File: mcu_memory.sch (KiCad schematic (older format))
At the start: 43 parts, among them J1 Conn_02x03_Odd_Even, P10 CONN_02X20, U2 STM32F429IGTx

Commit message: Corrected pinout of lateral IDC 40 pin. Moved other bits to another port
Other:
- note added: "OPTIMIZED FOR BUS ACCESS"
- note added: "PORTD 8 pins (SHIELD)"
- note added: "PORTE 6 pins (SHIELD)"
- note removed: "PORTD 13 pins (SHIELD)"
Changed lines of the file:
@@
 NoConn ~ 9900 5050
 NoConn ~ 9900 5150
-NoConn ~ 9900 8750
-NoConn ~ 9900 8850
-NoConn ~ 9900 8950
-NoConn ~ 9900 9050
-NoConn ~ 9900 9150
 NoConn ~ 9900 9250
 NoConn ~ 9900 9350
@@
 Text Notes 3400 8675 1    60   ~ 12
 PORTG 8 bit
-Text Notes 10425 8200 1    60   ~ 12
-PORTD 13 pins (SHIELD)
+Text Notes 10450 7900 1    60   ~ 12
+PORTD 8 pins (SHIELD)
 Wire Notes Line
 	3525 8950 3425 8950
@@
 Wire Notes Line
 	1050 7400 1050 10650
-Text GLabel 9900 7850 2    39   BiDi ~ 0
+Text GLabel 9900 8750 2    39   BiDi ~ 0
 D8
-Text GLabel 9900 7950 2    39   BiDi ~ 0
+Text GLabel 9900 8850 2    39   BiDi ~ 0
 D9
-Text GLabel 9900 8050 2    39   BiDi ~ 0
+Text GLabel 9900 8950 2    39   BiDi ~ 0
 D10
-Text GLabel 9900 8150 2    39   BiDi ~ 0
+Text GLabel 9900 9050 2    39   BiDi ~ 0
 D11
-Text GLabel 9900 8250 2    39   BiDi ~ 0
+Text GLabel 9900 9150 2    39   BiDi ~ 0
 D12
-Wire Notes Line
-	10075 7050 10300 7050
-Wire Notes Line
-	10300 7050 10300 8250
-Wire Notes Line
-	10300 8250 10125 8250
+NoConn ~ 9900 7850
+NoConn ~ 9900 7950
+NoConn ~ 9900 8050
+NoConn ~ 9900 8150
+NoConn ~ 9900 8250
+Wire Notes Line
+	10075 7050 10325 7050
+Wire Notes Line
+	10325 7050 10325 7750
+Wire Notes Line
+	10325 7750 10075 7750
+Wire Notes Line
+	10100 8750 10325 8750
+Wire Notes Line
+	10325 8750 10325 9150
+Wire Notes Line
+	10325 9150 10100 9150
+Text Notes 10475 9475 1    60   ~ 12
+PORTE 6 pins (SHIELD)
+Text Notes 10625 8000 1    59   ~ 12
+OPTIMIZED FOR BUS ACCESS
 $EndSCHEMATC

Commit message: Porting from Kicad 4 to Kicad 5
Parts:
- BOOT0_MEM1, BOOT1_MEM1: footprint Pin_Headers:Pin_Header_Straight_1x02 -> Connector_PinHeader_2.54mm:PinHeader_1x02_P2.54mm_Vertical; symbol CONN_01X02 -> stduinof429-rescue:CONN_01X02
- C10, C11, C12, C13, C14, C15, C16, C17, C18, C19, C20, C21, C22, C23, C24, C25, C26, C5, C6, C7, C8, C9: footprint Capacitors_SMD:C_1206_HandSoldering -> Capacitor_SMD:C_1206_3216Metric_Pad1.42x1.75mm_HandSolder; symbol C_Small -> Device1:C_Small
- D2: footprint LEDs:LED_1206 -> LED_SMD:LED_1206_3216Metric_Pad1.42x1.75mm_HandSolder; symbol Led_Small -> stduinof429-rescue:Led_Small
- DEBUG1: footprint Pin_Headers:Pin_Header_Straight_1x03 -> Connector_PinHeader_2.54mm:PinHeader_1x03_P2.54mm_Vertical; symbol CONN_01X03 -> stduinof429-rescue:CONN_01X03
- J1: symbol Conn_02x03_Odd_Even -> Connector_Generic1:Conn_02x03_Odd_Even
- P10: symbol CONN_02X20 -> stduinof429-rescue:CONN_02X20
- R10, R11, R12, R13, R14, R3, R4, R5, R6, R7, R8, R9: footprint Resistors_SMD:R_1206_HandSoldering -> Resistor_SMD:R_1206_3216Metric_Pad1.42x1.75mm_HandSolder; symbol R_Small -> Device1:R_Small
- SWDIO/CLK1: footprint Pin_Headers:Pin_Header_Angled_1x04 -> Connector_PinHeader_2.54mm:PinHeader_1x04_P2.54mm_Horizontal; symbol CONN_01X04 -> stduinof429-rescue:CONN_01X04
- U2: footprint Housings_QFP:LQFP-176_24x24mm_Pitch0.5mm -> Package_QFP:LQFP-176_24x24mm_P0.5mm; symbol STM32F429IGTx -> MCU_ST_STM32F41:STM32F429IGTx
- XT1: symbol Crystal_Small -> Device1:Crystal_Small

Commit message: Added without the packages/kicad folder needed. All stuff is now on kicad sources and RetroBitLab Library
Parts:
- BOOT0_MEM1, BOOT1_MEM1: symbol stduinof429-rescue:CONN_01X02 -> stduinof429-rescue:CONN_01X02-stduinof429-rescue
- C10, C11, C12, C13, C14, C15, C16, C17, C18, C19, C20, C21, C22, C23, C24, C25, C26, C5, C6, C7, C8, C9: symbol Device1:C_Small -> stduinof429-rescue:C_Small-Device1-stduinof429-rescue
- D2: symbol stduinof429-rescue:Led_Small -> stduinof429-rescue:Led_Small-stduinof429-rescue
- DEBUG1: symbol stduinof429-rescue:CONN_01X03 -> stduinof429-rescue:CONN_01X03-stduinof429-rescue
- J1: symbol Connector_Generic1:Conn_02x03_Odd_Even -> stduinof429-rescue:Conn_02x03_Odd_Even-Connector_Generic1-stduinof429-rescue
- P10: symbol stduinof429-rescue:CONN_02X20 -> stduinof429-rescue:CONN_02X20-stduinof429-rescue
- R10, R11, R12, R13, R14, R3, R4, R5, R6, R7, R8, R9: symbol Device1:R_Small -> stduinof429-rescue:R_Small-Device1-stduinof429-rescue
- SWDIO/CLK1: symbol stduinof429-rescue:CONN_01X04 -> stduinof429-rescue:CONN_01X04-stduinof429-rescue
- U2: symbol MCU_ST_STM32F41:STM32F429IGTx -> stduinof429-rescue:STM32F429IGTx-MCU_ST_STM32F41-stduinof429-rescue
- XT1: symbol Device1:Crystal_Small -> stduinof429-rescue:Crystal_Small-Device1-stduinof429-rescue
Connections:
- wire segments 164 -> 232

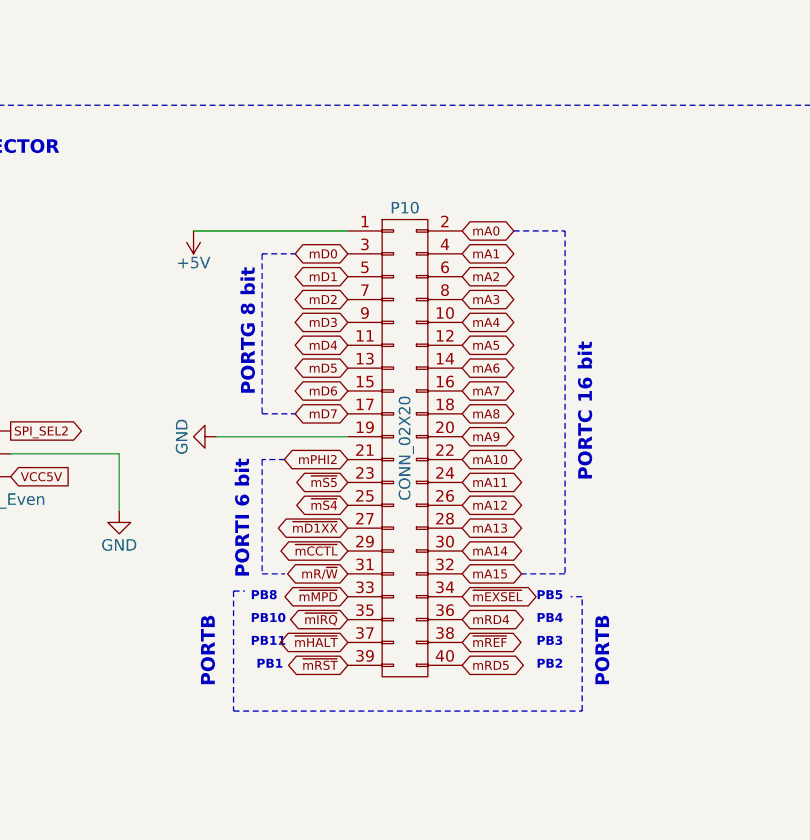
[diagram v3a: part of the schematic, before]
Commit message: Modified for Kicad 5.1.9
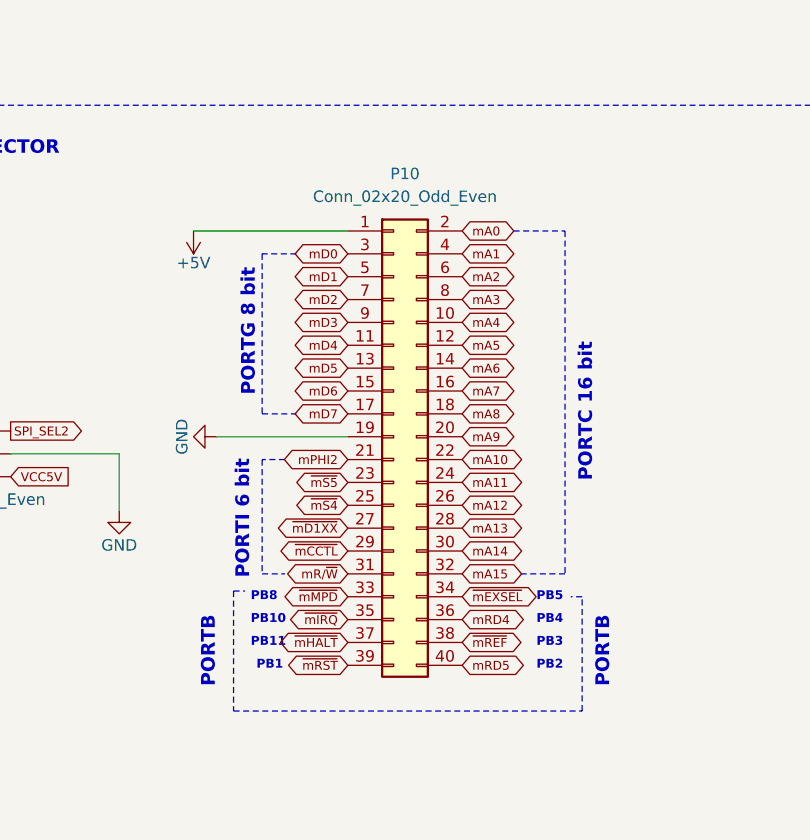
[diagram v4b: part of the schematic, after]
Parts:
- removed P10: CONN_02X20, RetroBitLab:IDC_02X20_2.54mm_Horizontal_PCB_2SIDES, symbol stduinof429-rescue:CONN_02X20-stduinof429-rescue
- added P10: Conn_02x20_Odd_Even, RetroBitLab:IDC_02X20_2.54mm_Horizontal_PCB_2SIDES, symbol Connector_Generic:Conn_02x20_Odd_Even
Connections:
- net +5V: now also P10.1 (Pin_1)
- net GND: now also P10.19 (Pin_19)
- net mA0: now also P10.2 (Pin_2)
- net mA1: now also P10.4 (Pin_4)
- net mA10: now also P10.22 (Pin_22)
- net mA11: now also P10.24 (Pin_24)
- net mA12: now also P10.26 (Pin_26)
- net mA13: now also P10.28 (Pin_28)
- net mA14: now also P10.30 (Pin_30)
- net mA15: now also P10.32 (Pin_32)
- net mA2: now also P10.6 (Pin_6)
- net mA3: now also P10.8 (Pin_8)
- net mA4: now also P10.10 (Pin_10)
- net mA5: now also P10.12 (Pin_12)
- net mA6: now also P10.14 (Pin_14)
- net mA7: now also P10.16 (Pin_16)
- net mA8: now also P10.18 (Pin_18)
- net mA9: now also P10.20 (Pin_20)
- net mD0: now also P10.3 (Pin_3)
- net mD1: now also P10.5 (Pin_5)
- net mD2: now also P10.7 (Pin_7)
- net mD3: now also P10.9 (Pin_9)
- net mD4: now also P10.11 (Pin_11)
- net mD5: now also P10.13 (Pin_13)
- net mD6: now also P10.15 (Pin_15)
- net mD7: now also P10.17 (Pin_17)
- net mPHI2: now also P10.21 (Pin_21)
- net mR/~W: now also P10.31 (Pin_31)
- net mRD4: now also P10.36 (Pin_36)
- net mRD5: now also P10.40 (Pin_40)
- net ~mCCTL: now also P10.29 (Pin_29)
- net ~mD1XX: now also P10.27 (Pin_27)
- net ~mEXSEL: now also P10.34 (Pin_34)
- net ~mHALT: now also P10.37 (Pin_37)
- net ~mIRQ: now also P10.35 (Pin_35)
- net ~mMPD: now also P10.33 (Pin_33)
- net ~mREF: now also P10.38 (Pin_38)
- net ~mRST: now also P10.39 (Pin_39)
- net ~mS4: now also P10.25 (Pin_25)
- net ~mS5: now also P10.23 (Pin_23)
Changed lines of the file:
@@
 Wire Wire Line
 	3800 7950 3125 7950
-$Comp
-L stduinof429-rescue:CONN_02X20-stduinof429-rescue P10
-U 1 1 5DA3A653
-P 4050 8900
-F 0 "P10" H 4050 9950 50  0000 C CNN
-F 1 "CONN_02X20" V 4050 8900 50  0000 C CNN
-F 2 "RetroBitLab:IDC_02X20_2.54mm_Horizontal_PCB_2SIDES" H 4050 7950 50  0001 C CNN
-F 3 "" H 4050 7950 50  0000 C CNN
-	1    4050 8900
-	1    0    0    -1
-$EndComp
 Wire Notes Line
 	3300 9525 3300 10050
@@
 Wire Wire Line
 	14500 600  14700 600
+$Comp
+L Connector_Generic:Conn_02x20_Odd_Even P10
+U 1 1 605B226E
+P 4000 8850
+F 0 "P10" H 4050 10000 50  0000 C CNN
+F 1 "Conn_02x20_Odd_Even" H 4050 9900 50  0000 C CNN
+F 2 "RetroBitLab:IDC_02X20_2.54mm_Horizontal_PCB_2SIDES" H 4000 8850 50  0001 C CNN
+F 3 "~" H 4000 8850 50  0001 C CNN
+	1    4000 8850
+	1    0    0    -1
+$EndComp
 $EndSCHEMATC

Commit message: Created for rescue :-(
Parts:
- BOOT0_MEM1, BOOT1_MEM1: symbol stduinof429-rescue:CONN_01X02-stduinof429-rescue -> stduinof429-rescue:CONN_01X02-stduinof429-rescue-stduinof429-rescue
- C10, C11, C12, C13, C14, C15, C16, C17, C18, C19, C20, C21, C22, C23, C24, C25, C26, C5, C6, C7, C8, C9: symbol stduinof429-rescue:C_Small-Device1-stduinof429-rescue -> stduinof429-rescue:C_Small-Device1-stduinof429-rescue-stduinof429-rescue
- D2: symbol stduinof429-rescue:Led_Small-stduinof429-rescue -> stduinof429-rescue:Led_Small-stduinof429-rescue-stduinof429-rescue
- DEBUG1: symbol stduinof429-rescue:CONN_01X03-stduinof429-rescue -> stduinof429-rescue:CONN_01X03-stduinof429-rescue-stduinof429-rescue
- J1: symbol stduinof429-rescue:Conn_02x03_Odd_Even-Connector_Generic1-stduinof429-rescue -> stduinof429-rescue:Conn_02x03_Odd_Even-Connector_Generic1-stduinof429-rescue-stduinof429-rescue
- R10, R11, R12, R13, R14, R3, R4, R5, R6, R7, R8, R9: symbol stduinof429-rescue:R_Small-Device1-stduinof429-rescue -> stduinof429-rescue:R_Small-Device1-stduinof429-rescue-stduinof429-rescue
- SWDIO/CLK1: symbol stduinof429-rescue:CONN_01X04-stduinof429-rescue -> stduinof429-rescue:CONN_01X04-stduinof429-rescue-stduinof429-rescue
- U2: symbol stduinof429-rescue:STM32F429IGTx-MCU_ST_STM32F41-stduinof429-rescue -> stduinof429-rescue:STM32F429IGTx-MCU_ST_STM32F41-stduinof429-rescue-stduinof429-rescue
- XT1: symbol stduinof429-rescue:Crystal_Small-Device1-stduinof429-rescue -> stduinof429-rescue:Crystal_Small-Device1-stduinof429-rescue-stduinof429-rescue
